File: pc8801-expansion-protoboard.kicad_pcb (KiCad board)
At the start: 2 copper layers, 219 x 95 mm, 36 parts, among them J1 Solder Side, J2 Parts Side, J3 5V, J4 12V, J5 -12V, J6 GND_1, J7 GND_2, U1 ExpansionEdge, U10 74LS165, U11 ESP32-DEVKITC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

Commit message: Bad FujiNet
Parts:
- added D1: LED, LED_THT:LED_D3.0mm, F.Cu at (213.6, 99.1)
- added R2: 560Ω, Resistor_THT:R_Axial_DIN0207_L6.3mm_D2.5mm_P10.16mm_Horizontal, F.Cu at (208.0, 109.2)
- added R3: 10kΩ, Resistor_THT:R_Axial_DIN0204_L3.6mm_D1.6mm_P7.62mm_Horizontal, F.Cu at (172.5, 66.0)
- moved R1 0.90 mm to (124.0, 105.7)
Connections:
- net /~A7 renamed /~{A7}
- net /~FUJI_CS renamed /~{FUJI_CS}
- net /~FUJI_RD renamed /~{SPI_RD}
- net /~FUJI_SEL renamed /~{SPI_IFACE_SEL}
- net /~FUJI_WR renamed /~{SPI_WR}
- net /~IOR renamed /~{IOR}
- net /~IOW renamed /~{IOW}
- net /~SD_CS renamed /~{SD_CS}
- net /~SER_RD renamed /~{SER_RD}
- net /~SER_WR renamed /~{SER_WR}
- net /~SPI_CLK renamed /~{SPI_CLK}
- net /~START renamed /~{START}
- net /~VSPI_SS renamed /~{VSPI_SS}
- net Net-(U7-Pad6) renamed /CS_ON
- net Net-(U7-Pad7) renamed /CS_OFF
- U10 pad 7: Net-(U10-Pad7) -> unconnected-(U10-Pad7)
- U11 pad 10: Net-(U11-Pad10) -> unconnected-(U11-Pad10)
- U11 pad 11: Net-(U11-Pad11) -> unconnected-(U11-Pad11)
- U11 pad 12: Net-(U11-Pad12) -> unconnected-(U11-Pad12)
- U11 pad 13: Net-(U11-Pad13) -> unconnected-(U11-Pad13)
- U11 pad 15: Net-(U11-Pad15) -> unconnected-(U11-Pad15)
- U11 pad 16: Net-(U11-Pad16) -> unconnected-(U11-Pad16)
- U11 pad 17: Net-(U11-Pad17) -> unconnected-(U11-Pad17)
- U11 pad 18: Net-(U11-Pad18) -> unconnected-(U11-Pad18)
- U11 pad 20: Net-(U11-Pad20) -> unconnected-(U11-Pad20)
- U11 pad 21: Net-(U11-Pad21) -> unconnected-(U11-Pad21)
- U11 pad 22: Net-(U11-Pad22) -> unconnected-(U11-Pad22)
- U11 pad 23: Net-(U11-Pad23) -> unconnected-(U11-Pad23)
- U11 pad 24: Net-(U11-Pad24) -> unconnected-(U11-Pad24)
- U11 pad 26: Net-(U11-Pad26) -> unconnected-(U11-Pad26)
- U11 pad 27: Net-(U11-Pad27) -> unconnected-(U11-Pad27)
- U11 pad 28: Net-(U11-Pad28) -> unconnected-(U11-Pad28)
- U11 pad 3: Net-(U11-Pad3) -> unconnected-(U11-Pad3)
- U11 pad 33: Net-(U11-Pad33) -> unconnected-(U11-Pad33)
- U11 pad 34: Net-(U11-Pad34) -> unconnected-(U11-Pad34)
- U11 pad 35: Net-(U11-Pad35) -> unconnected-(U11-Pad35)
- U11 pad 36: Net-(U11-Pad36) -> unconnected-(U11-Pad36)
- U11 pad 4: Net-(U11-Pad4) -> unconnected-(U11-Pad4)
- U11 pad 5: Net-(U11-Pad5) -> unconnected-(U11-Pad5)
- U11 pad 6: Net-(U11-Pad6) -> unconnected-(U11-Pad6)
- U11 pad 7: Net-(U11-Pad7) -> unconnected-(U11-Pad7)
- U11 pad 8: Net-(U11-Pad8) -> unconnected-(U11-Pad8)
- U11 pad 9: Net-(U11-Pad9) -> unconnected-(U11-Pad9)
- U5 pad 11: Net-(U5-Pad11) -> unconnected-(U5-Pad11)
- U5 pad 12: Net-(U5-Pad12) -> unconnected-(U5-Pad12)
- U5 pad 13: Net-(U5-Pad13) -> unconnected-(U5-Pad13)
- U5 pad 3: Net-(U5-Pad3) -> unconnected-(U5-Pad3)
- U5 pad 4: Net-(U5-Pad4) -> unconnected-(U5-Pad4)
- U5 pad 5: Net-(U5-Pad5) -> unconnected-(U5-Pad5)
- U5 pad 6: Net-(U5-Pad6) -> unconnected-(U5-Pad6)
- U7 pad 11: Net-(U7-Pad11) -> unconnected-(U7-Pad11)
- U9 pad 9: Net-(U9-Pad9) -> unconnected-(U9-Pad9)
- X1 pad 1: Net-(X1-Pad1) -> unconnected-(X1-Pad1)
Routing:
- net /+5V: track 459.1 -> 423.1 mm, vias 21 -> 20
- net /GND: track 426.5 -> 455.1 mm, vias 17 -> 16
- net Net-(R2-Pad1): track 0.00 -> 12.8 mm, vias 0 -> 1
- net Net-(U11-Pad2): track 0.00 -> 8.70 mm
- net Net-(U11-Pad1): track 0.00 -> 6.61 mm
- net Net-(D1-Pad2): track 0.00 -> 3.05 mm
- net Net-(R1-Pad1): track 81.8 -> 82.7 mm
- net /FUJI_OUT: track 143.3 -> 144.1 mm
- net /SPI_CLK: vias 8 -> 7
- net /A6: vias 4 -> 3
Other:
- net class Default removed
- board text added: "3v3"
- board text added: "CS"
- board text added: "~{CLK}"
- board text added: "~{CS}"
- board text added: "~{M1}"
- board text added: "~{NMI}"
- board text added: "~{RD}"
- board text added: "~{RESET}"
- board text added: "~{ROM KILL}"
- board text added: "~{SLAVE_SELECT}"
- board text added: "~{WAITRQ}"
- board text added: "~{WE}"
- board text added: "~{WR}"
- board text removed: "~CLK"
- board text removed: "~CS"
- board text removed: "~M1"
- board text removed: "~NMI"
- board text removed: "~RD"
- board text removed: "~RESET"
- board text removed: "~ROM KILL"
- board text removed: "~SLAVE_SELECT"
- board text removed: "~WAITRQ"
- board text removed: "~WE"
- board text removed: "~WR"

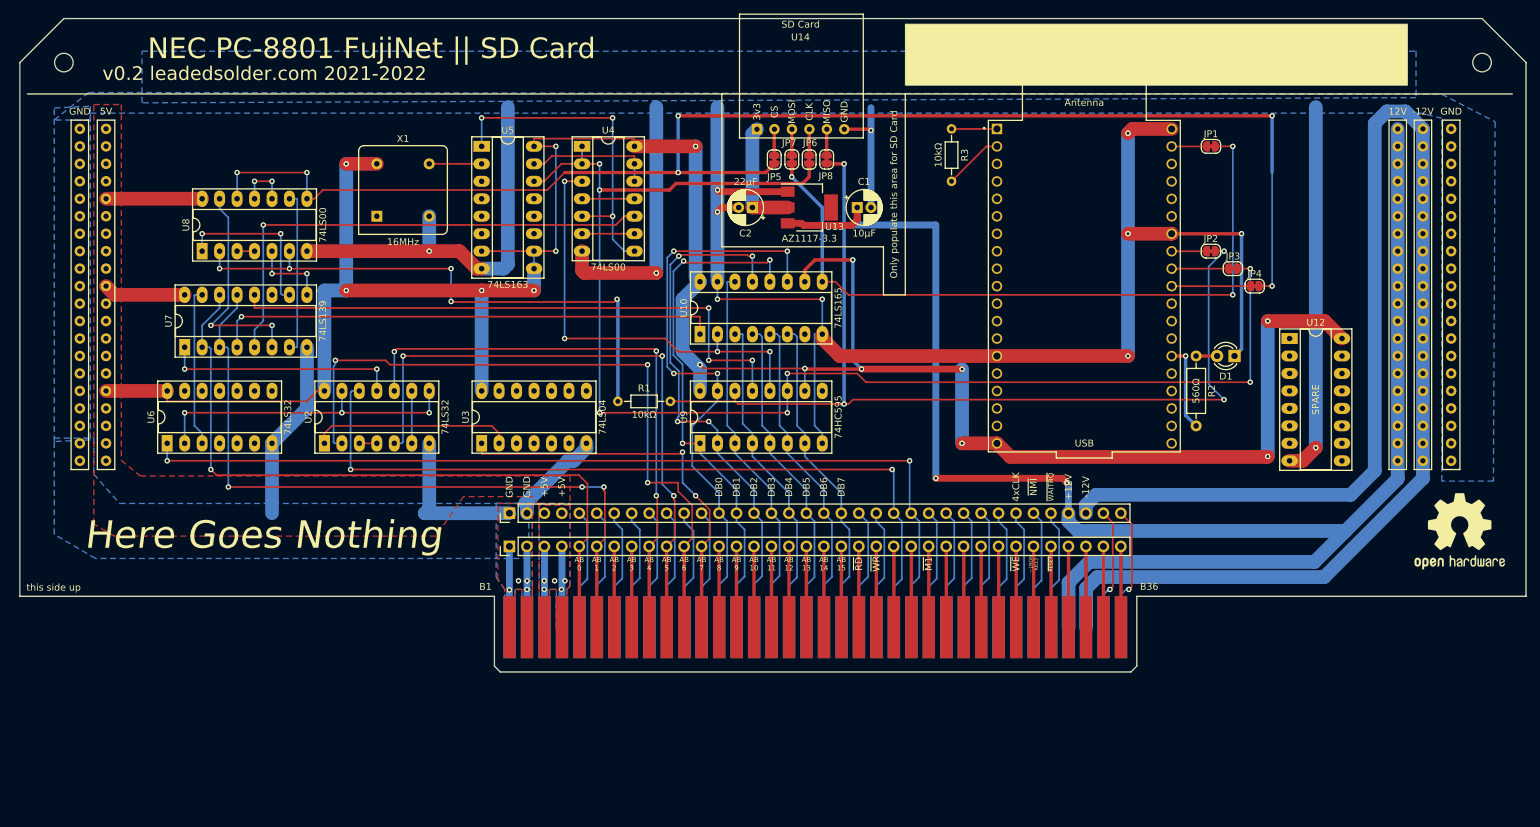
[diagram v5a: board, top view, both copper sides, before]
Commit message: Fix swapped-side near disaster
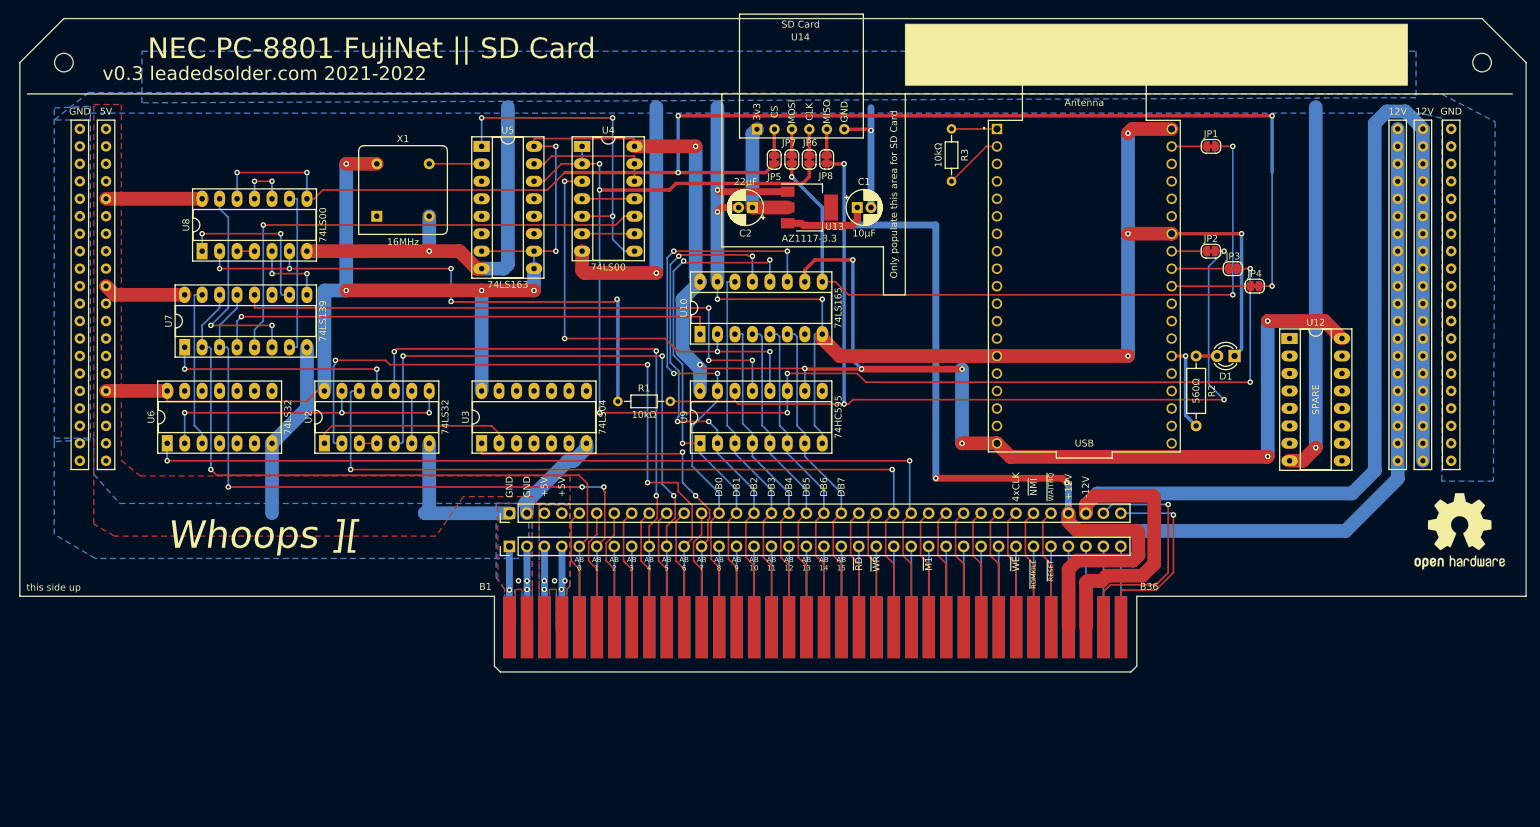
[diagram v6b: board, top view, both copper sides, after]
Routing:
- net /-12V: track 216.6 -> 191.8 mm
- net Net-(J2-Pad35): track 17.8 -> 35.6 mm
- net /+12V: track 241.5 -> 226.4 mm
- net Net-(J2-Pad36): track 18.1 -> 30.1 mm
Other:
- board text added: "Whoops ]["
- board text added: "v0.3 leadedsolder.com 2021-2022"
- board text added: "~{ROMKILL}"
- board text removed: "Here Goes Nothing"
- board text removed: "v0.2 leadedsolder.com 2021-2022"
- board text removed: "~{ROM KILL}"

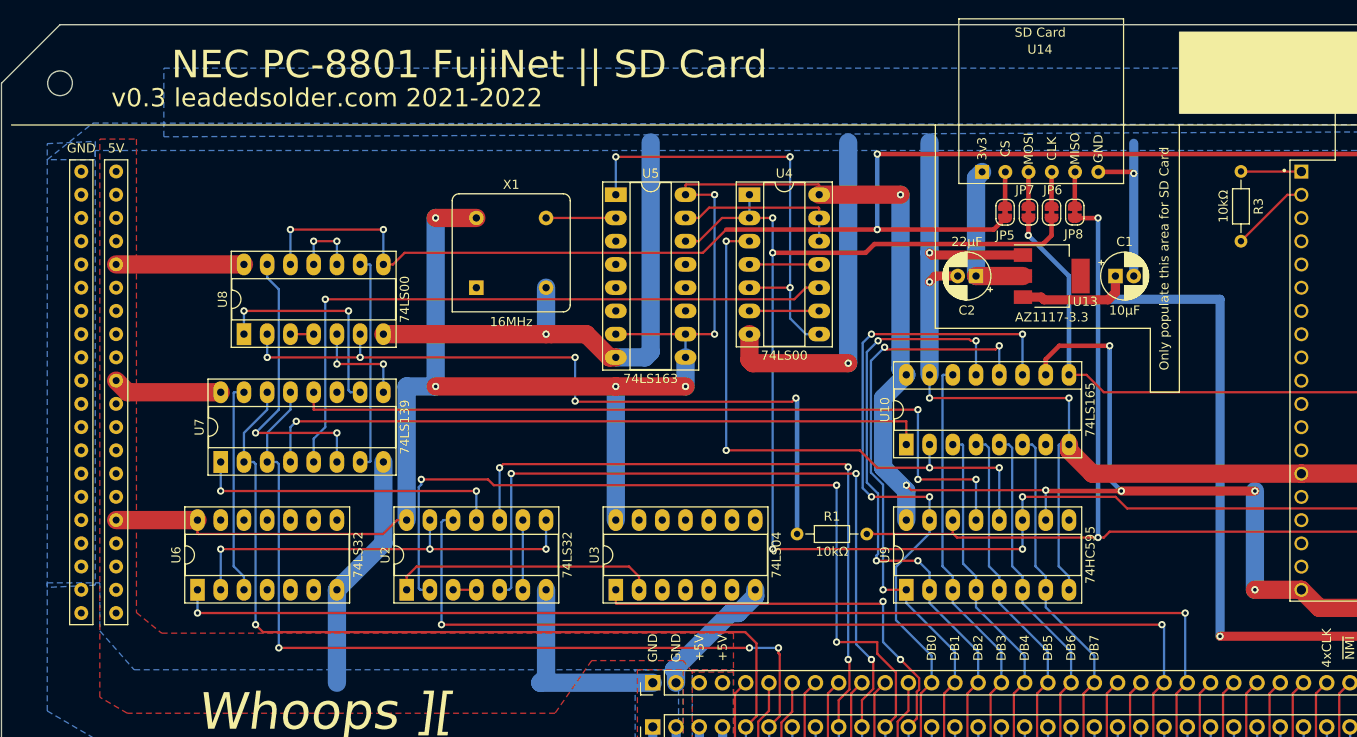
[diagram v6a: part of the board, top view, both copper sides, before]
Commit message: Rewire and add test points
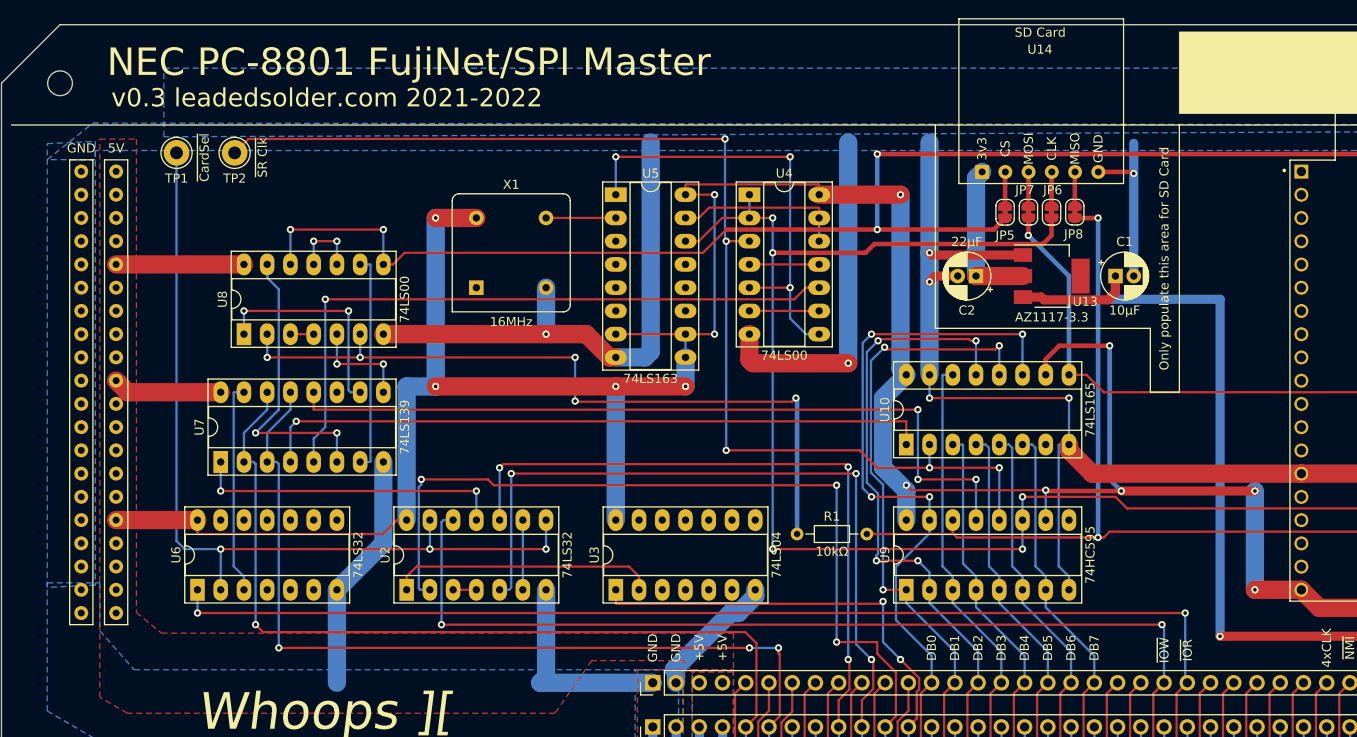
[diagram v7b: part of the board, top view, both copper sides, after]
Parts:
- removed R3: 10kΩ, Resistor_THT:R_Axial_DIN0204_L3.6mm_D1.6mm_P7.62mm_Horizontal
- added TP1: TestPoint, TestPoint:TestPoint_Loop_D2.60mm_Drill1.4mm_Beaded, F.Cu at (56.1, 64.0)
- added TP2: TestPoint, TestPoint:TestPoint_Loop_D2.60mm_Drill1.4mm_Beaded, F.Cu at (62.5, 64.0)
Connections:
- net Net-(J1-Pad24) renamed /~{IORQ}
- net Net-(J1-Pad31) renamed /~{ROMKILL}
- U11 pad 1: Net-(U11-Pad1) -> unconnected-(U11-Pad1)
- U11 pad 2: Net-(U11-Pad2) -> unconnected-(U11-Pad2)
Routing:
- net /~{SPI_CLK}: track 64.3 -> 129.7 mm, vias 4 -> 5
- net /~{SPI_IFACE_SEL}: track 46.4 -> 94.0 mm
- net Net-(U11-Pad2): track 8.70 -> 0.00 mm
- net Net-(U11-Pad1): track 6.61 -> 0.00 mm
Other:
- board text added: "NEC PC-8801 FujiNet/SPI Master"
- board text added: "~{CardSel}"
- board text added: "~{IOR}"
- board text added: "~{IOW}"
- board text added: "~{SR Clk}"
- board text removed: "NEC PC-8801 FujiNet || SD Card"

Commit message: V0.2 for FujiNet sent to JLCPCB
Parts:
- added D2: LED, LED_THT:LED_D3.0mm, F.Cu at (216.4, 105.7)
- added R3: 560Ω, Resistor_THT:R_Axial_DIN0207_L6.3mm_D2.5mm_P10.16mm_Horizontal, F.Cu at (211.1, 102.1)
- moved D1 0.51 mm to (213.6, 98.6)
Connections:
- U11 pad 24: unconnected-(U11-Pad24) -> Net-(U11-Pad24)
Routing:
- net Net-(D2-Pad2): track 0.00 -> 7.66 mm
- net /GND: track 455.1 -> 462.7 mm
- net Net-(U11-Pad24): track 0.00 -> 6.81 mm
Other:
- board text added: "(Green)"
- board text added: "(Red)"
